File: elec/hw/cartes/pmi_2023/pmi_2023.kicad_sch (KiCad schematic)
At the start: 4 parts

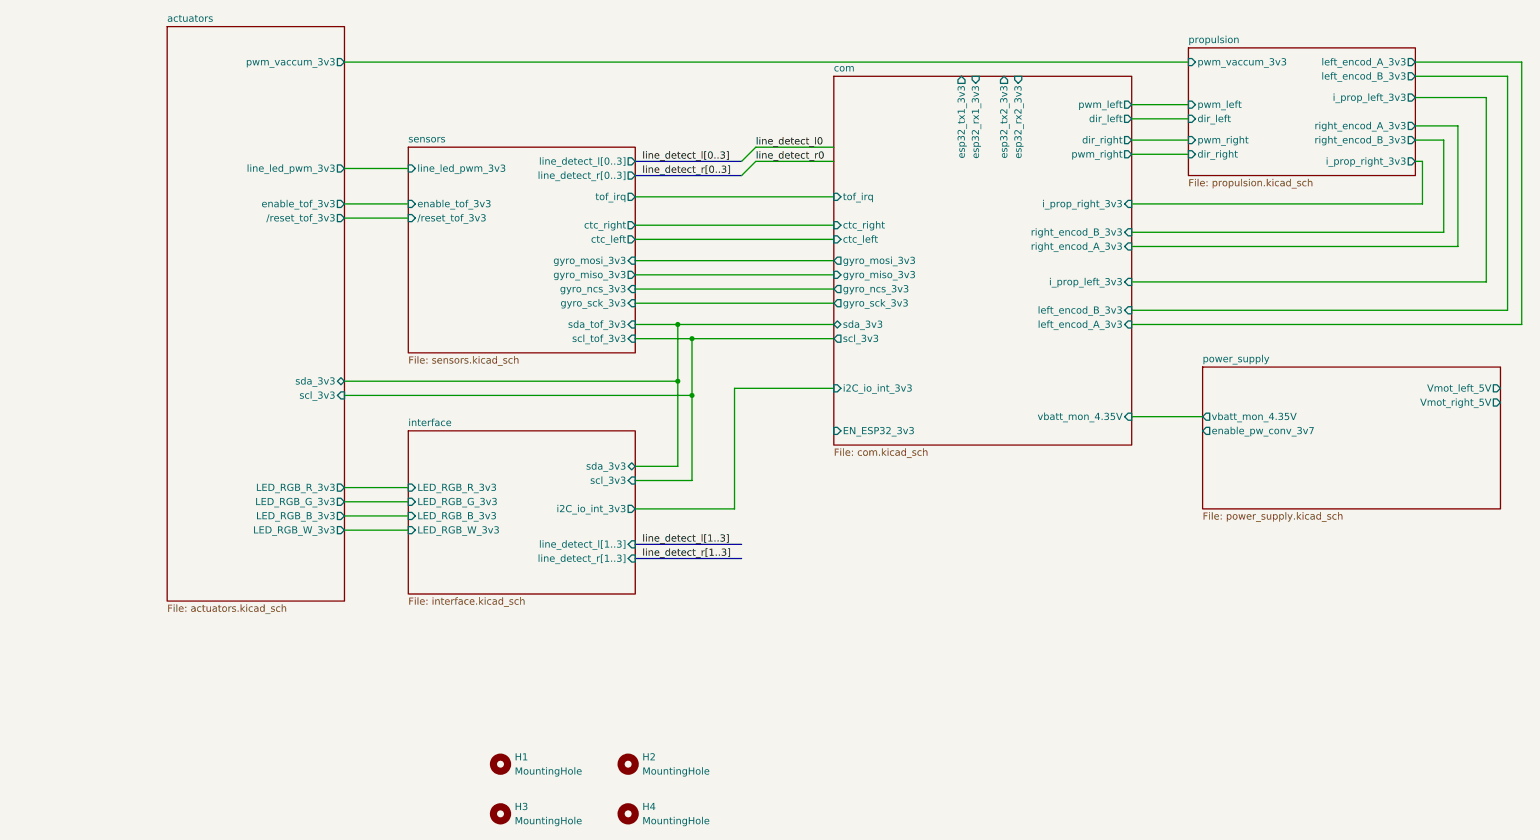
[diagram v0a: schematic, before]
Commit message: pmi layout (WIP)
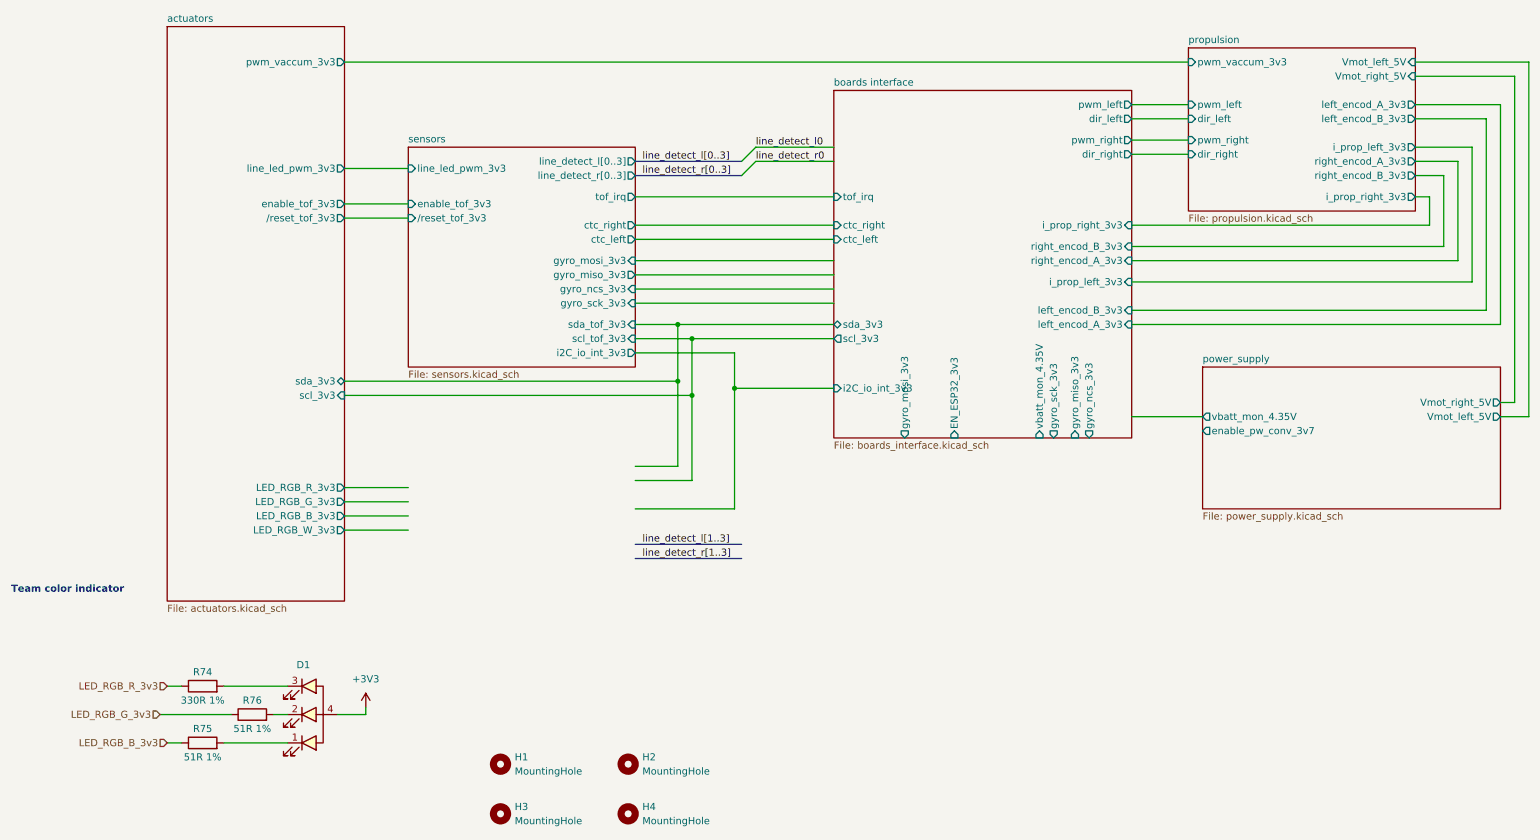
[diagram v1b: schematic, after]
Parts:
- added D1: ~, cocotter_diodes:3528_PLCC-Reverse_mount, symbol cocotter_diodes:IN-P32TRRRGB
- added R74: 330R 1%, cocotter_resistor:r0603_reflow, symbol cocotter_resistors:R_330R_0603_1%
- added R75, R76: 51R 1%, cocotter_resistor:r0603_reflow, symbol cocotter_resistors:R_51R_0603_1%
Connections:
- new net: D1.3 (C_RED), R74.2
- new net: D1.2 (C_GREEN), R76.2
- new net: D1.1 (C_BLUE), R75.2
- new net +3V3: D1.4 (COM)
- new net LED_RGB_B_3v3: R75.1
- new net LED_RGB_G_3v3: R76.1
- new net LED_RGB_R_3v3: R74.1
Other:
- removed sheet com
- removed sheet interface
- added sheet boards interface (boards_interface.kicad_sch)
- sheet propulsion ports: added Vmot_left_5V, Vmot_right_5V; removed none
- sheet sensors ports: added i2C_io_int_3v3; removed none
- note added: "Team color indicator"

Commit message: wip
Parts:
- removed D1: ~, cocotter_diodes:3528_PLCC-Reverse_mount, symbol cocotter_diodes:IN-P32TRRRGB
- removed R74: 330R 1%, cocotter_resistor:r0603_reflow, symbol cocotter_resistors:R_330R_0603_1%
- removed R75, R76: 51R 1%, cocotter_resistor:r0603_reflow, symbol cocotter_resistors:R_51R_0603_1%
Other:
- sheet actuators ports: added none; removed LED_RGB_B_3v3, LED_RGB_G_3v3, LED_RGB_R_3v3, LED_RGB_W_3v3
- sheet boards interface ports: added none; removed EN_ESP32_3v3, gyro_miso_3v3, gyro_mosi_3v3, gyro_ncs_3v3, gyro_sck_3v3, vbatt_mon_4.35V
- sheet sensors ports: added none; removed gyro_miso_3v3, gyro_mosi_3v3, gyro_ncs_3v3, gyro_sck_3v3

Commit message: wip
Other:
- sheet boards interface ports: added vbatt_mon_4.35V; removed none
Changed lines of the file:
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@@
+		)
+	)
+	(wire
+		(pts
+			(xy 274.32 54.61) (xy 274.32 93.98)
+		)
+		(stroke
+			(width 0)
+			(type default)
+		)
+	)
+	(wire
+		(pts
+			(xy 69.85 104.14) (xy 129.54 104.14)
+		)
+		(stroke
+			(width 0)
+			(type default)
+		)
+	)
+	(wire
+		(pts
+			(xy 271.78 91.44) (xy 210.82 91.44)
+		)
+		(stroke
+			(width 0)
+			(type default)
+		)
+	)
+	(wire
+		(pts
+			(xy 69.85 46.99) (xy 218.44 46.99)
+		)
+		(stroke
+			(width 0)
+			(type default)
+		)
+	)
+	(wire
+		(pts
+			(xy 69.85 66.04) (xy 81.28 66.04)
+		)
+		(stroke
+			(width 0)
+			(type default)
+		)
+	)
+	(wire
+		(pts
+			(xy 129.54 93.98) (xy 157.48 93.98)
+		)
+		(stroke
+			(width 0)
+			(type default)
+		)
+	)
+	(wire
+		(pts
+			(xy 121.92 78.74) (xy 157.48 78.74)
+		)
+		(stroke
+			(width 0)
+			(type default)
+		)
+	)
+	(wire
+		(pts
+			(xy 143.51 64.77) (xy 157.48 64.77)
+		)
+		(stroke
+			(width 0)
+			(type default)
+		)
+	)
+	(wire
+		(pts
+			(xy 210.82 54.61) (xy 218.44 54.61)
+		)
+		(stroke
+			(width 0)
+			(type default)
+		)
+	)
+	(wire
+		(pts
+			(xy 271.78 57.15) (xy 271.78 91.44)
+		)
+		(stroke
+			(width 0)
+			(type default)
 		)
 	)
 	(bus
 		(pts
-			(xy 121.92 135.89) (xy 140.97 135.89)
-		)
-		(stroke
-			(width 0)
-			(type default)
-		)
-	)
-	(wire
-		(pts
-			(xy 274.32 54.61) (xy 274.32 93.98)
-		)
-		(stroke
-			(width 0)
-			(type default)
-		)
-	)
-	(wire
-		(pts
-			(xy 69.85 104.14) (xy 129.54 104.14)
-		)
-		(stroke
-			(width 0)
-			(type default)
-		)
-	)
-	(wire
-		(pts
-			(xy 271.78 91.44) (xy 210.82 91.44)
-		)
-		(stroke
-			(width 0)
-			(type default)
-		)
-	)
-	(wire
-		(pts
-			(xy 69.85 46.99) (xy 218.44 46.99)
-		)
-		(stroke
-			(width 0)
-			(type default)
-		)
-	)
-	(wire
-		(pts
-			(xy 69.85 66.04) (xy 81.28 66.04)
-		)
-		(stroke
-			(width 0)
-			(type default)
-		)
-	)
-	(wire
-		(pts
-			(xy 129.54 93.98) (xy 157.48 93.98)
-		)
-		(stroke
-			(width 0)
-			(type default)
-		)
-	)
-	(wire
-		(pts
-			(xy 121.92 78.74) (xy 157.48 78.74)
-		)
-		(stroke
-			(width 0)
-			(type default)
-		)
-	)
-	(wire
-		(pts
-			(xy 143.51 64.77) (xy 157.48 64.77)
-		)
-		(stroke
-			(width 0)
-			(type default)
-		)
-	)
-	(wire
-		(pts
-			(xy 210.82 54.61) (xy 218.44 54.61)
-		)
-		(stroke
-			(width 0)
-			(type default)
-		)
-	)
-	(wire
-		(pts
-			(xy 271.78 57.15) (xy 271.78 91.44)
+			(xy 121.92 64.77) (xy 140.97 64.77)
+		)
+		(stroke
+			(width 0)
+			(type default)
+		)
+	)
+	(wire
+		(pts
+			(xy 132.08 96.52) (xy 132.08 106.68)
+		)
+		(stroke
+			(width 0)
+			(type default)
+		)
+	)
+	(wire
+		(pts
+			(xy 259.08 67.31) (xy 264.16 67.31)
+		)
+		(stroke
+			(width 0)
+			(type default)
+		)
+	)
+	(wire
+		(pts
+			(xy 132.08 96.52) (xy 157.48 96.52)
+		)
+		(stroke
+			(width 0)
+			(type default)
+		)
+	)
+	(wire
+		(pts
+			(xy 264.16 80.01) (xy 210.82 80.01)
+		)
+		(stroke
+			(width 0)
+			(type default)
+		)
+	)
+	(wire
+		(pts
+			(xy 210.82 60.96) (xy 218.44 60.96)
 		)
 		(stroke
@@
 	(bus
 		(pts
-			(xy 121.92 64.77) (xy 140.97 64.77)
-		)
-		(stroke
-			(width 0)
-			(type default)
-		)
-	)
-	(wire
-		(pts
-			(xy 132.08 96.52) (xy 132.08 106.68)
-		)
-		(stroke
-			(width 0)
-			(type default)
-		)
-	)
-	(wire
-		(pts
-			(xy 259.08 67.31) (xy 264.16 67.31)
-		)
-		(stroke
-			(width 0)
-			(type default)
-		)
-	)
-	(wire
-		(pts
-			(xy 132.08 96.52) (xy 157.48 96.52)
-		)
-		(stroke
-			(width 0)
-			(type default)
-		)
-	)
-	(wire
-		(pts
-			(xy 264.16 80.01) (xy 210.82 80.01)
-		)
-		(stroke
-			(width 0)
-			(type default)
-		)
-	)
-	(wire
-		(pts
-			(xy 210.82 60.96) (xy 218.44 60.96)
-		)
-		(stroke
-			(width 0)
-			(type default)
-		)
-	)
-	(bus
-		(pts
 			(xy 121.92 67.31) (xy 140.97 67.31)
 		)
@@
 		(pts
 			(xy 210.82 76.2) (xy 261.62 76.2)
-		)
-		(stroke
-			(width 0)
-			(type default)
-		)
-	)
-	(bus
-		(pts
-			(xy 121.92 133.35) (xy 140.97 133.35)
 		)
 		(stroke
@@
 		)
 	)
-	(label "line_detect_l[1..3]"
-		(at 123.19 133.35 0)
-		(fields_autoplaced yes)
-		(effects
-			(font
-				(size 1.27 1.27)
-			)
-			(justify left bottom)
-		)
-	)
 	(label "line_detect_l0"
 		(at 143.51 62.23 0)
-		(fields_autoplaced yes)
-		(effects
-			(font
-				(size 1.27 1.27)
-			)
-			(justify left bottom)
-		)
-	)
-	(label "line_detect_r[1..3]"
-		(at 123.19 135.89 0)
 		(fields_autoplaced yes)
 		(effects
@@
 			)
 		)
-		(property "Description" ""
+		(property "Description" "Mounting Hole without connection"
 			(at 120.65 181.61 0)
 			(effects
@@
 			)
 		)
-		(property "Description" ""
+		(property "Description" "Mounting Hole without connection"
 			(at 120.65 172.72 0)
 			(effects
@@
 			)
 		)
-		(property "Description" ""
+		(property "Description" "Mounting Hole without connection"
 			(at 97.79 172.72 0)
 			(effects
@@
 			)
 		)
-		(property "Description" ""
+		(property "Description" "Mounting Hole without connection"
 			(at 97.79 181.61 0)
 			(effects
@@
 			)
 		)
+		(pin "vbatt_mon_4.35V" input
+			(at 210.82 110.49 0)
+			(effects
+				(font
+					(size 1.27 1.27)
+				)
+				(justify right)
+			)
+		)

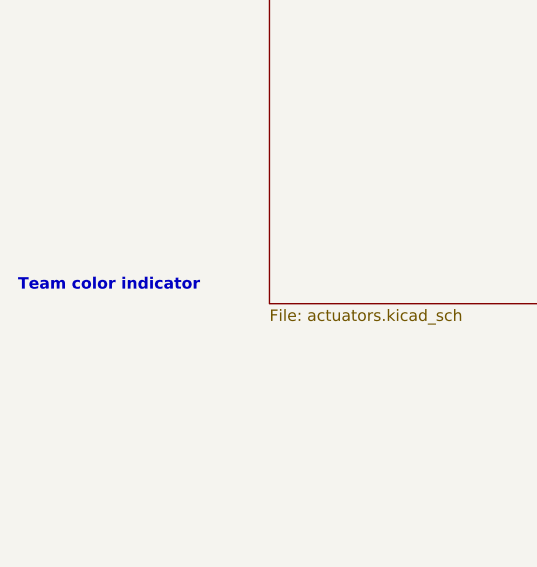
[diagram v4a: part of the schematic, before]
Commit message: added oled display power supply res selectors, jlcpcb refs : wip
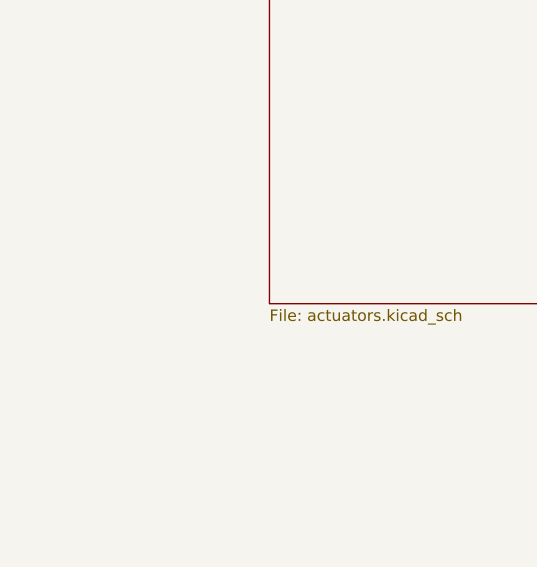
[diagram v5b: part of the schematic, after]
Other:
- note removed: "Team color indicator"
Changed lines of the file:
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@@
-		)
-	)
-	(text "Team color indicator"
-		(exclude_from_sim no)
-		(at 10.16 142.24 0)
-		(effects
-			(font
-				(size 1.27 1.27)
-				(thickness 0.254)
-				(bold yes)
-			)
-			(justify left bottom)
 		)
 	)

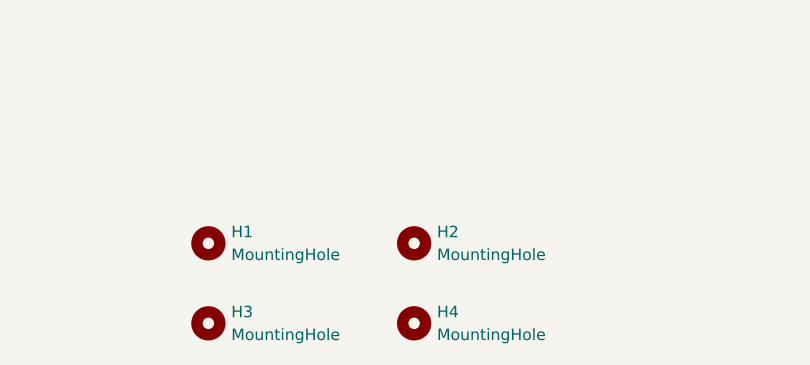
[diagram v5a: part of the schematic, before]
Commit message: reset button added to esp32 reset. uart prog connector replaces ftdi one
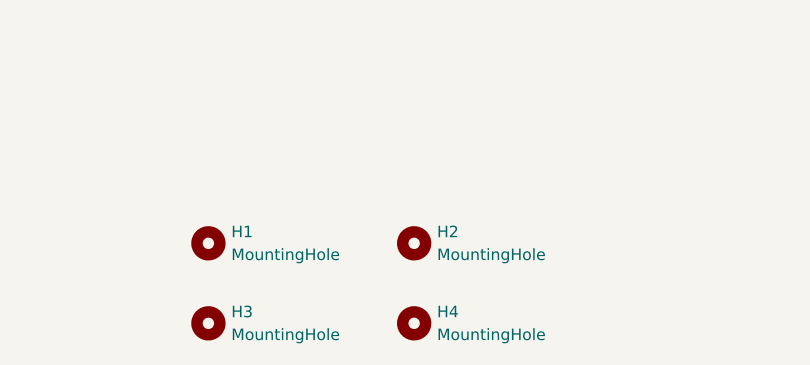
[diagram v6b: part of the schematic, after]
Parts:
- H1, H2, H3, H4: footprint MountingHole:MountingHole_2.1mm -> (none); now left out of the parts list
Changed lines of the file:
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@@
 		(at 120.65 181.61 0)
 		(unit 1)
-		(exclude_from_sim no)
-		(in_bom yes)
+		(exclude_from_sim yes)
+		(in_bom no)
 		(on_board yes)
 		(dnp no)
 		(fields_autoplaced yes)
 		(property "Reference" "H4"
-			(at 123.19 180.34 0)
-			(effects
-				(font
-					(size 1.27 1.27)
-				)
-				(justify left)
-			)
-		)
-		(property "Value" "MountingHole"
-			(at 123.19 182.88 0)
-			(effects
-				(font
-					(size 1.27 1.27)
-				)
-				(justify left)
-			)
-		)
-		(property "Footprint" "MountingHole:MountingHole_2.1mm"
+			(at 123.19 180.3399 0)
+			(effects
+				(font
+					(size 1.27 1.27)
+				)
+				(justify left)
+			)
+		)
+		(property "Value" "MountingHole"
+			(at 123.19 182.8799 0)
+			(effects
+				(font
+					(size 1.27 1.27)
+				)
+				(justify left)
+			)
+		)
+		(property "Footprint" ""
 			(at 120.65 181.61 0)
 			(effects
@@
 		(at 120.65 172.72 0)
 		(unit 1)
-		(exclude_from_sim no)
-		(in_bom yes)
+		(exclude_from_sim yes)
+		(in_bom no)
 		(on_board yes)
 		(dnp no)
 		(fields_autoplaced yes)
 		(property "Reference" "H2"
-			(at 123.19 171.45 0)
-			(effects
-				(font
-					(size 1.27 1.27)
-				)
-				(justify left)
-			)
-		)
-		(property "Value" "MountingHole"
-			(at 123.19 173.99 0)
-			(effects
-				(font
-					(size 1.27 1.27)
-				)
-				(justify left)
-			)
-		)
-		(property "Footprint" "MountingHole:MountingHole_2.1mm"
+			(at 123.19 171.4499 0)
+			(effects
+				(font
+					(size 1.27 1.27)
+				)
+				(justify left)
+			)
+		)
+		(property "Value" "MountingHole"
+			(at 123.19 173.9899 0)
+			(effects
+				(font
+					(size 1.27 1.27)
+				)
+				(justify left)
+			)
+		)
+		(property "Footprint" ""
 			(at 120.65 172.72 0)
 			(effects
@@
 		(at 97.79 172.72 0)
 		(unit 1)
-		(exclude_from_sim no)
-		(in_bom yes)
+		(exclude_from_sim yes)
+		(in_bom no)
 		(on_board yes)
 		(dnp no)
 		(fields_autoplaced yes)
 		(property "Reference" "H1"
-			(at 100.33 171.45 0)
-			(effects
-				(font
-					(size 1.27 1.27)
-				)
-				(justify left)
-			)
-		)
-		(property "Value" "MountingHole"
-			(at 100.33 173.99 0)
-			(effects
-				(font
-					(size 1.27 1.27)
-				)
-				(justify left)
-			)
-		)
-		(property "Footprint" "MountingHole:MountingHole_2.1mm"
+			(at 100.33 171.4499 0)
+			(effects
+				(font
+					(size 1.27 1.27)
+				)
+				(justify left)
+			)
+		)
+		(property "Value" "MountingHole"
+			(at 100.33 173.9899 0)
+			(effects
+				(font
+					(size 1.27 1.27)
+				)
+				(justify left)
+			)
+		)
+		(property "Footprint" ""
 			(at 97.79 172.72 0)
 			(effects
@@
 		(at 97.79 181.61 0)
 		(unit 1)
-		(exclude_from_sim no)
-		(in_bom yes)
+		(exclude_from_sim yes)
+		(in_bom no)
 		(on_board yes)
 		(dnp no)
 		(fields_autoplaced yes)
 		(property "Reference" "H3"
-			(at 100.33 180.34 0)
-			(effects
-				(font
-					(size 1.27 1.27)
-				)
-				(justify left)
-			)
-		)
-		(property "Value" "MountingHole"
-			(at 100.33 182.88 0)
-			(effects
-				(font
-					(size 1.27 1.27)
-				)
-				(justify left)
-			)
-		)
-		(property "Footprint" "MountingHole:MountingHole_2.1mm"
+			(at 100.33 180.3399 0)
+			(effects
+				(font
+					(size 1.27 1.27)
+				)
+				(justify left)
+			)
+		)
+		(property "Value" "MountingHole"
+			(at 100.33 182.8799 0)
+			(effects
+				(font
+					(size 1.27 1.27)
+				)
+				(justify left)
+			)
+		)
+		(property "Footprint" ""
 			(at 97.79 181.61 0)
 			(effects

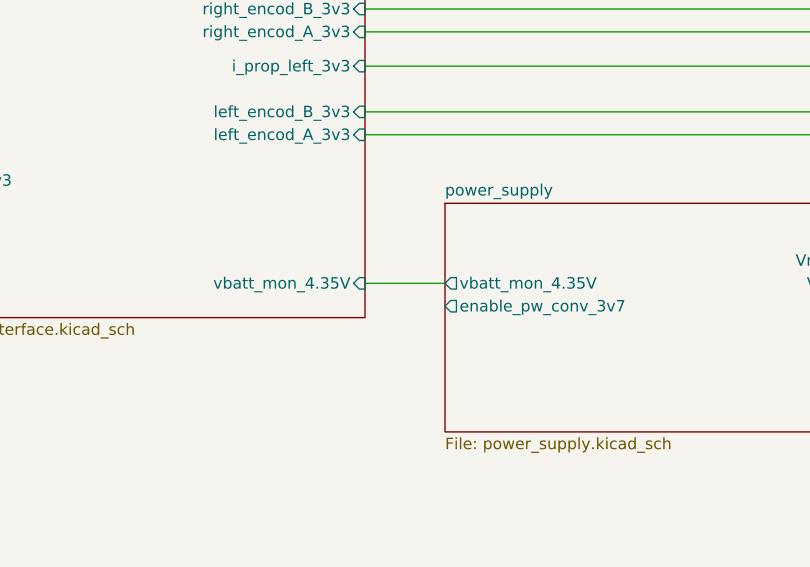
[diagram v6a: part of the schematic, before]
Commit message: routing cleanup, test points added to allow charging of battery in the pmi
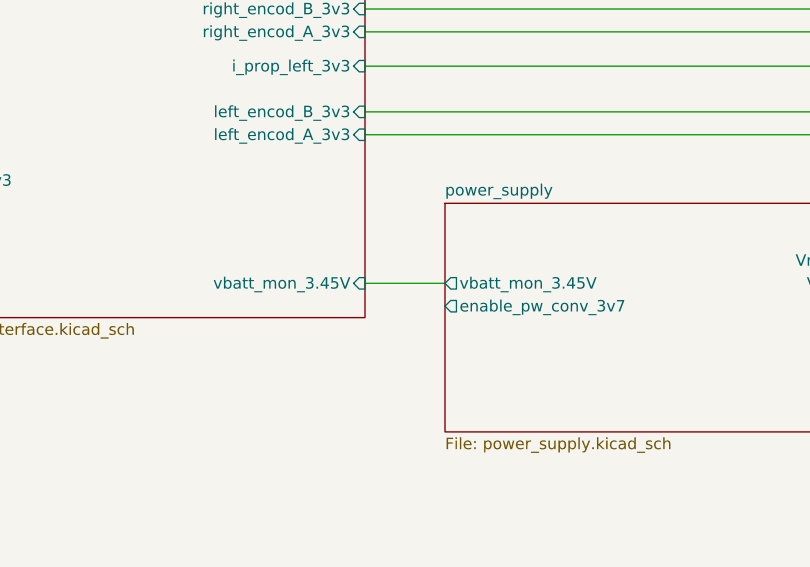
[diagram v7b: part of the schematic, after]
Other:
- sheet boards interface ports: added vbatt_mon_3.45V; removed vbatt_mon_4.35V
- sheet power_supply ports: added vbatt_mon_3.45V; removed vbatt_mon_4.35V
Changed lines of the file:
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@@
 			)
 		)
-		(pin "vbatt_mon_4.35V" output
+		(pin "vbatt_mon_3.45V" output
 			(at 219.71 110.49 180)
 			(effects
@@
 			)
 		)
-		(pin "vbatt_mon_4.35V" input
+		(pin "vbatt_mon_3.45V" input
 			(at 210.82 110.49 0)
 			(effects

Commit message: small changes
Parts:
- H1, H2, H3, H4: footprint (none) -> cocotter_others:MountingHole_2.1mm
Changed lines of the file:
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@@
 			)
 		)
-		(property "Footprint" ""
+		(property "Footprint" "cocotter_others:MountingHole_2.1mm"
 			(at 120.65 181.61 0)
 			(effects
@@
 			)
 		)
-		(property "Footprint" ""
+		(property "Footprint" "cocotter_others:MountingHole_2.1mm"
 			(at 120.65 172.72 0)
 			(effects
@@
 			)
 		)
-		(property "Footprint" ""
+		(property "Footprint" "cocotter_others:MountingHole_2.1mm"
 			(at 97.79 172.72 0)
 			(effects
@@
 			)
 		)
-		(property "Footprint" ""
+		(property "Footprint" "cocotter_others:MountingHole_2.1mm"
 			(at 97.79 181.61 0)
 			(effects
